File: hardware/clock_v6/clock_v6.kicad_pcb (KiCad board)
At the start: 2 copper layers, 130 x 70 mm, 241 parts, among them J1 RJ45, J12 Conn_01x06, J2 Conn_01x06_Pin, J3 Conn_01x05_Pin, J4 Conn_01x04_Pin, J5 Conn_01x06_Pin, J6 Conn_01x04_Pin, J7 Conn_01x04_Pin, J8 Conn_01x02, J9 Conn_02x10_Odd_Even, Q1 2N7002, Q10 2N7002, Q2 2N7002, Q3 2N7002, Q4 2N7002, Q5 2N7002, Q6 2N7002, Q7 2N7002, Q8 2N7002, Q9 2N7002, U1 ADA4807-1, U10 STM32F405RGTx, U11 AMS1117-3.3, U12 BA50DD0WHFP-TR, U13 M24C02-RMN, U2 SN74LVC1G14DBV, U3 SN74LVC1G14DBV, U4 ADA4807-1, U5 ADA4807-1, U6 TLV3603DCKR, U7 SN74LVC1G14DBV, U8 TLV3603DCKR, U9 L78L05_SOT89, X2 GTXO-14V (2.048MHz), Y1 AOCJY4A-10.000MHZ-SW, Y2 16MHz

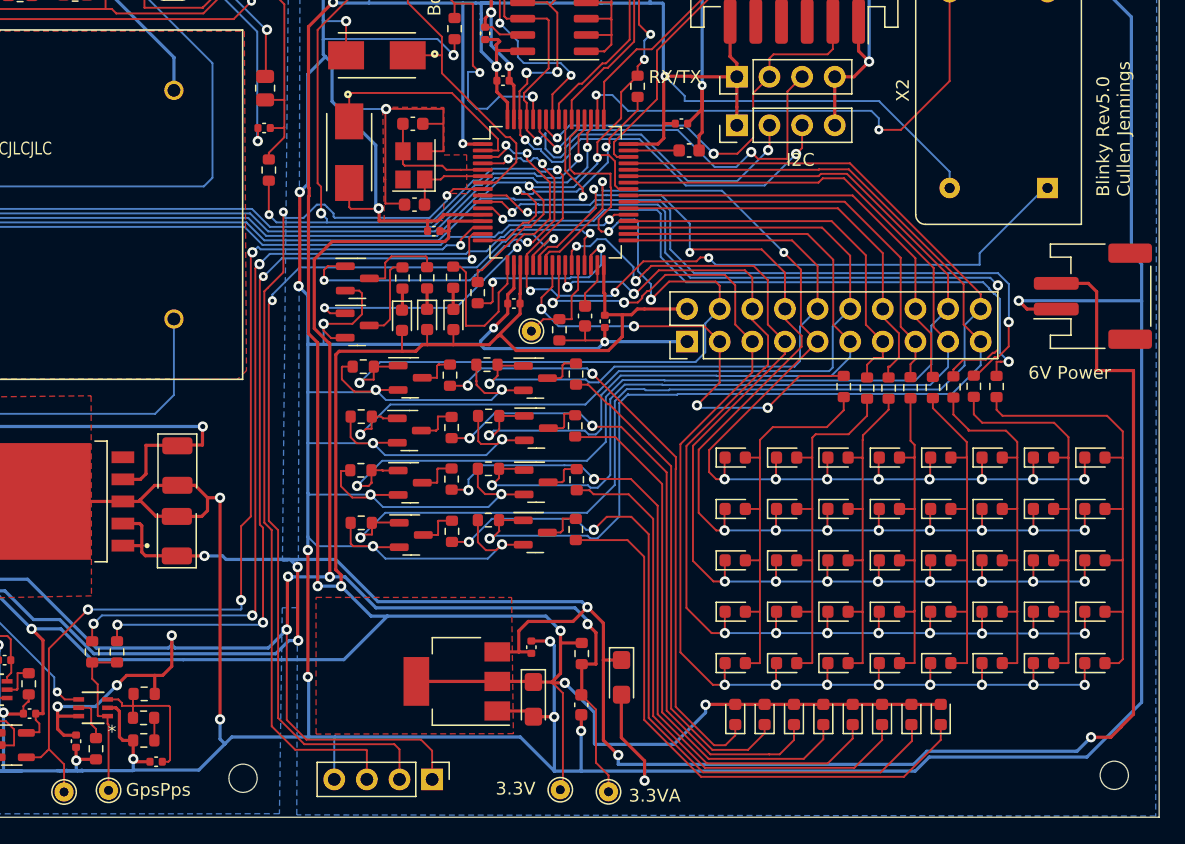
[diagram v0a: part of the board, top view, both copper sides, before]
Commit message: start cleaning up clock PCB
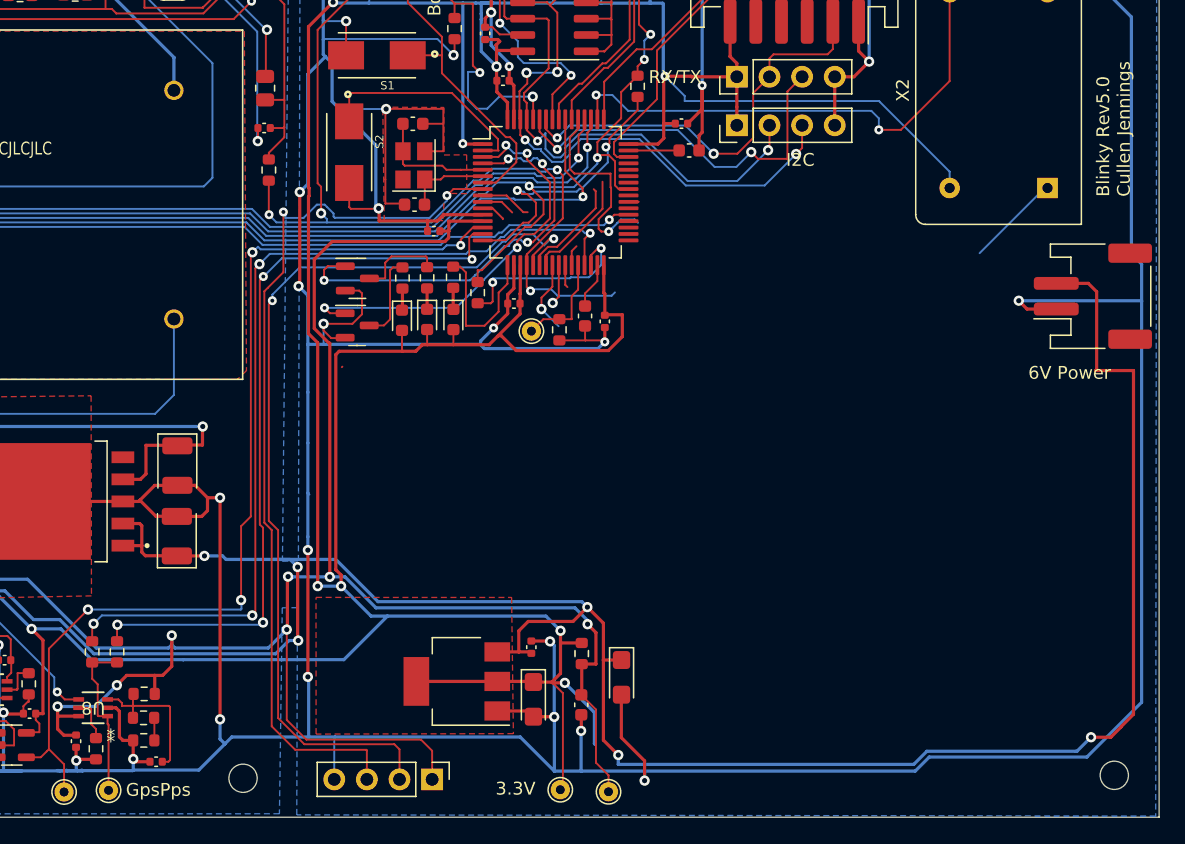
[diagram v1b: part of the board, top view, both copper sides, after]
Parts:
- removed D10, D11, D4, D5, D6, D7, D8, D9: LED-RED, LED_SMD:LED_0603_1608Metric
- removed D12, D13, D14, D15, D16, D17, D18, D19, D20, D21, D22, D23, D24, D25, D26, D27, D28, D29, D30, D31, D32, D33, D34, D35, D36, D37, D38, D39, D40, D41, D42, D43, D44, D45, D46, D47, D48, D49, D50, D51: LED-G, LED_SMD:LED_0603_1608Metric
- removed J9: Conn_02x10_Odd_Even, Connector_PinHeader_2.54mm:PinHeader_2x10_P2.54mm_Vertical
- removed Q1, Q2, Q3, Q4, Q5, Q6, Q7, Q8: 2N7002, Package_TO_SOT_SMD:SOT-23
- removed R33, R35, R37, R39, R41, R43, R45, R47: 4K7, Resistor_SMD:R_0603_1608Metric
- removed R34, R36, R38, R40, R42, R44, R46, R48: 100R, Resistor_SMD:R_0603_1608Metric
- removed R49, R50, R51, R52, R53, R55, R56, R57: 82R, Resistor_SMD:R_0603_1608Metric
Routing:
- net GND: track 1188.4 -> 1071.5 mm, vias 59 -> 51
- net /LEDB: track 98.3 -> 0.00 mm, vias 1 -> 0
- net /COL3: track 96.3 -> 3.36 mm, vias 10 -> 1
- net /LEDD: track 90.8 -> 0.00 mm, vias 1 -> 0
- net /COL5: track 91.8 -> 1.78 mm, vias 10 -> 0
- net /LEDC: track 89.7 -> 0.00 mm, vias 1 -> 0
- net /COL4: track 89.4 -> 1.63 mm, vias 10 -> 0
- net /COL1: track 94.0 -> 8.21 mm, vias 10 -> 0
- net /COL2: track 90.3 -> 8.78 mm, vias 10 -> 0
- net /LEDE: track 81.5 -> 0.00 mm, vias 1 -> 0
- net /LEDF: track 70.4 -> 0.00 mm, vias 1 -> 0
- net /LEDG: track 61.4 -> 0.00 mm, vias 1 -> 0
- net /LB: track 56.4 -> 0.00 mm, vias 2 -> 0
- net /LD: track 53.6 -> 0.00 mm, vias 2 -> 0
- net /LEDH: track 52.4 -> 0.00 mm, vias 1 -> 0
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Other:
- board text removed: "3.3VA"

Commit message: final clean up
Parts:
- removed ANT6: U.FL-R-SMT-1, blinky_footprints:U.FL-R-SMT-1
- removed J3: Conn_01x05_Pin, Connector_PinHeader_2.54mm:PinHeader_1x05_P2.54mm_Vertical
- removed JP1: SolderJumper_2_Bridged, Jumper:SolderJumper-2_P1.3mm_Bridged_RoundedPad1.0x1.5mm
- removed RV1: 20K, Potentiometer_SMD:Potentiometer_Bourns_3314G_Vertical
- removed TP12, TP13, TP14: ~, TestPoint:TestPoint_THTPad_D1.5mm_Drill0.7mm
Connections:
- R12 pad 2: Net-(J3-Pin_4) -> /Vadj
- R13 pad 1: Net-(J3-Pin_4) -> /Vadj
- R23 pad 2: Net-(J3-Pin_4) -> /Vadj
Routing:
- net +3.3VA: track 229.6 -> 136.7 mm, vias 9 -> 7
- net Net-(J3-Pin_4): track 50.4 -> 0.00 mm, vias 4 -> 0
- net Net-(Y1-VREF): track 59.8 -> 36.7 mm
- net OSC_ADJ: track 76.6 -> 60.2 mm, vias 4 -> 3
- net /LEDA: track 15.8 -> 0.00 mm, vias 1 -> 0
- net Net-(C26-Pad1): track 21.6 -> 7.74 mm, vias 1 -> 0
- net GND: track 1071.5 -> 1062.3 mm, vias 51 -> 50
- net /COL2: track 8.78 -> 0.00 mm
- net /COL1: track 8.21 -> 0.00 mm
- net +3.3V: track 374.3 -> 367.5 mm, vias 16 -> 15
- net /BOOT0: track 24.5 -> 18.8 mm
- net /ROW5: track 5.66 -> 0.00 mm, vias 1 -> 0
- net /Vadj: track 49.4 -> 44.3 mm, vias 2 -> 4
- net /ROW6: track 4.04 -> 0.00 mm
- net /NRST: track 28.4 -> 24.6 mm
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
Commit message: remove cheap osc
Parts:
- removed TP11: ~, TestPoint:TestPoint_THTPad_D1.5mm_Drill0.7mm
- removed X2: GTXO-14V (2.048MHz), Oscillator:Oscillator_DIP-14
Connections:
- TP10 pad 1: AUX_CLK -> CLK
- U10 pad 14: AUX_CLK -> /AUX_CLK
- U10 pad 50: /CLK -> CLK
- U7 pad 4: AUX_CLK -> CLK
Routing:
- net AUX_CLK: track 77.2 -> 0.00 mm, vias 4 -> 0
- net (no net): track 0.00 -> 77.2 mm, vias 0 -> 4
- net CLK: track 0.00 -> 39.6 mm, vias 0 -> 2
- net /CLK: track 39.6 -> 0.00 mm, vias 2 -> 0

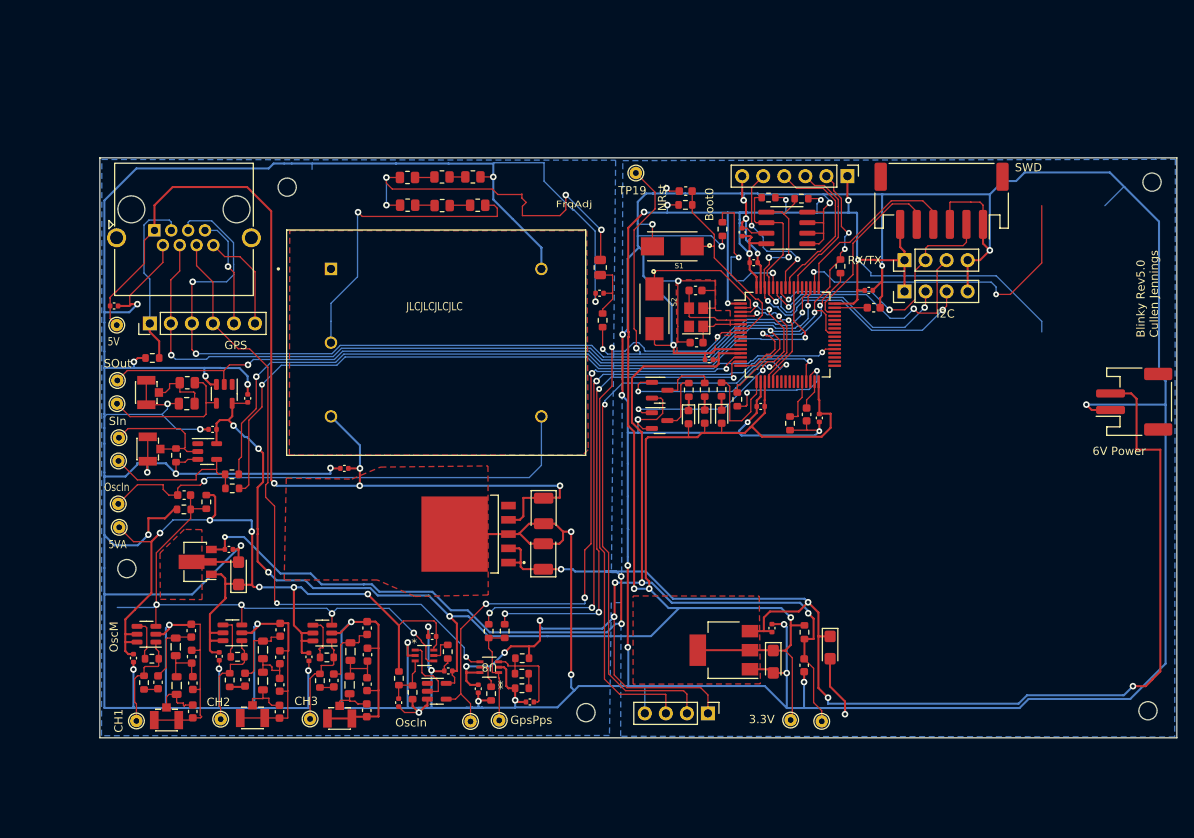
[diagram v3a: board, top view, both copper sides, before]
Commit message: clean up connections and add gps tx voltage dividers
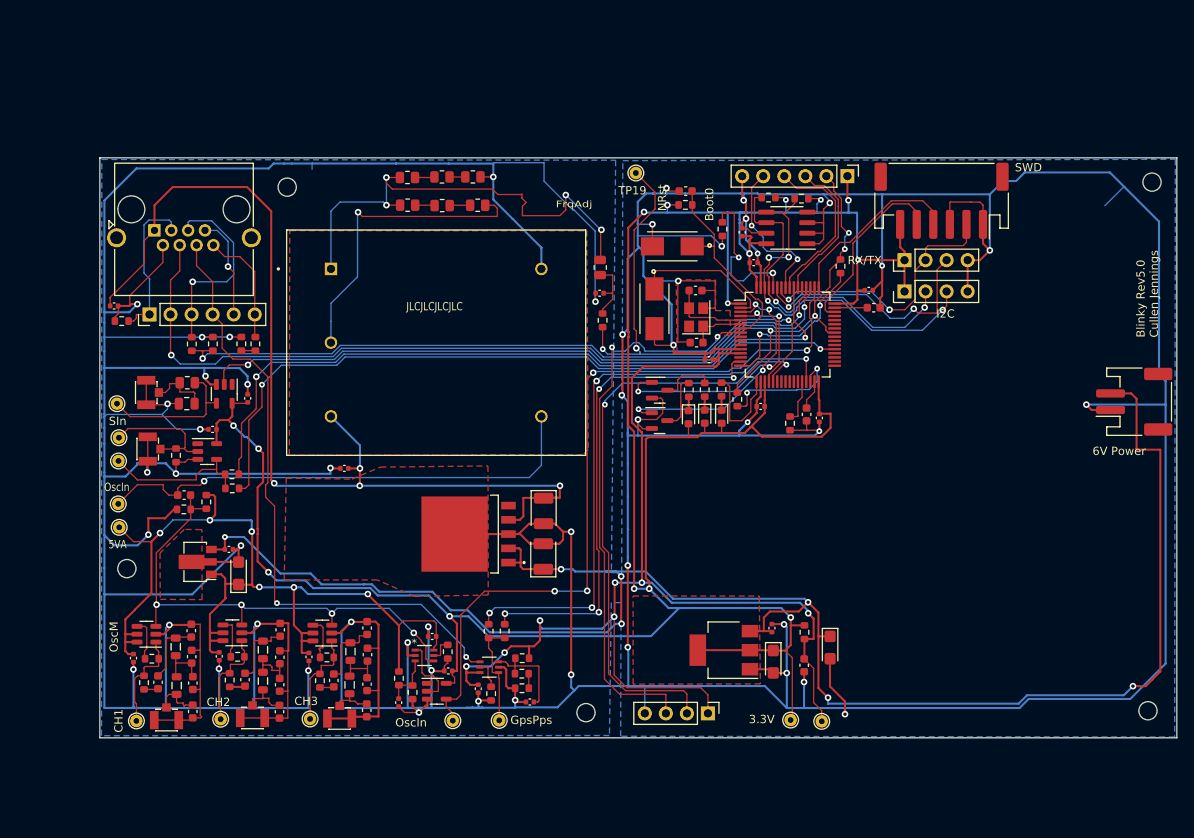
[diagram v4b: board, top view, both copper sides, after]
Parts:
- removed TP1, TP18: ~, TestPoint:TestPoint_THTPad_D1.5mm_Drill0.7mm
- added R33: 2K2, Resistor_SMD:R_0603_1608Metric, F.Cu at (118.8, 72.5)
- added R34: 4K7, Resistor_SMD:R_0603_1608Metric, F.Cu at (117.1, 72.4)
- added R35: 2K2, Resistor_SMD:R_0603_1608Metric, F.Cu at (111.1, 72.5)
- added R36: 4K7, Resistor_SMD:R_0603_1608Metric, F.Cu at (113.6, 72.5)
- moved R1 5.79 mm to (102.6, 69.7)
- moved TP10 2.14 mm to (142.6, 117.9)
- moved J2 1.08 mm to (106.0, 68.9)
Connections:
- net /GPS_TX2 renamed /GPS_TX2H
- J1 pad 5: /GPS_TX1 -> /GPS_TX1H
- J2 pad 3: /GPS_TX1 -> /GPS_TX1H
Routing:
- net (no net): track 77.2 -> 0.00 mm, vias 4 -> 0
- net CLK: track 39.6 -> 92.7 mm, vias 2 -> 4
- net +3.3V: track 367.5 -> 340.8 mm
- net /GPS_TX1H: track 0.00 -> 23.5 mm, vias 0 -> 1
- net /GPS_TX1: track 105.7 -> 82.9 mm, vias 3 -> 2
- net GND: track 1062.3 -> 1080.9 mm, vias 50 -> 51
- net SYNC_OUT: track 125.6 -> 109.6 mm
- net /Vadj: track 44.3 -> 58.6 mm
- net /10Mhz2.5V: track 65.8 -> 61.0 mm
- net +5V: track 122.2 -> 119.6 mm
- net /GPS_EN: track 21.5 -> 18.9 mm
- net /AUX_SYNC_MON: track 22.2 -> 20.2 mm
- net /GPS_TX2: track 0.00 -> 1.70 mm
- net /GPS_TX2H: track 12.6 -> 14.3 mm
- net /LEDM1: track 32.9 -> 31.6 mm
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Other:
- board text removed: "5V"
- board text removed: "GPS"
- board text removed: "SOut"

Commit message: resize board
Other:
- board size 130 x 70 mm -> 119 x 92 mm
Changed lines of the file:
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@@
     )
     (pad_to_mask_clearance 0)
-    (aux_axis_origin 100 120)
+    (aux_axis_origin 90 125)
     (pcbplotparams
       (layerselection 0x00010fc_ffffffff)
@@
     )
   )
-  (gr_line (start 230 120) (end 100 120)
+  (gr_line (start 209 125) (end 90 125)
     (stroke (width 0.1) (type default)) (layer "Edge.Cuts"))
-  (gr_line (start 100 50) (end 230 50)
+  (gr_line (start 90 33) (end 209 33)
     (stroke (width 0.1) (type default)) (layer "Edge.Cuts"))
-  (gr_line (start 230 50) (end 230 120)
+  (gr_line (start 209 33) (end 209 125)
     (stroke (width 0.1) (type default)) (layer "Edge.Cuts"))
-  (gr_line (start 100 50) (end 100 120)
+  (gr_line (start 90 33) (end 90 125)
     (stroke (width 0.1) (type default)) (layer "Edge.Cuts"))
   (gr_line (start 230 117.5) (end 100 117.5)

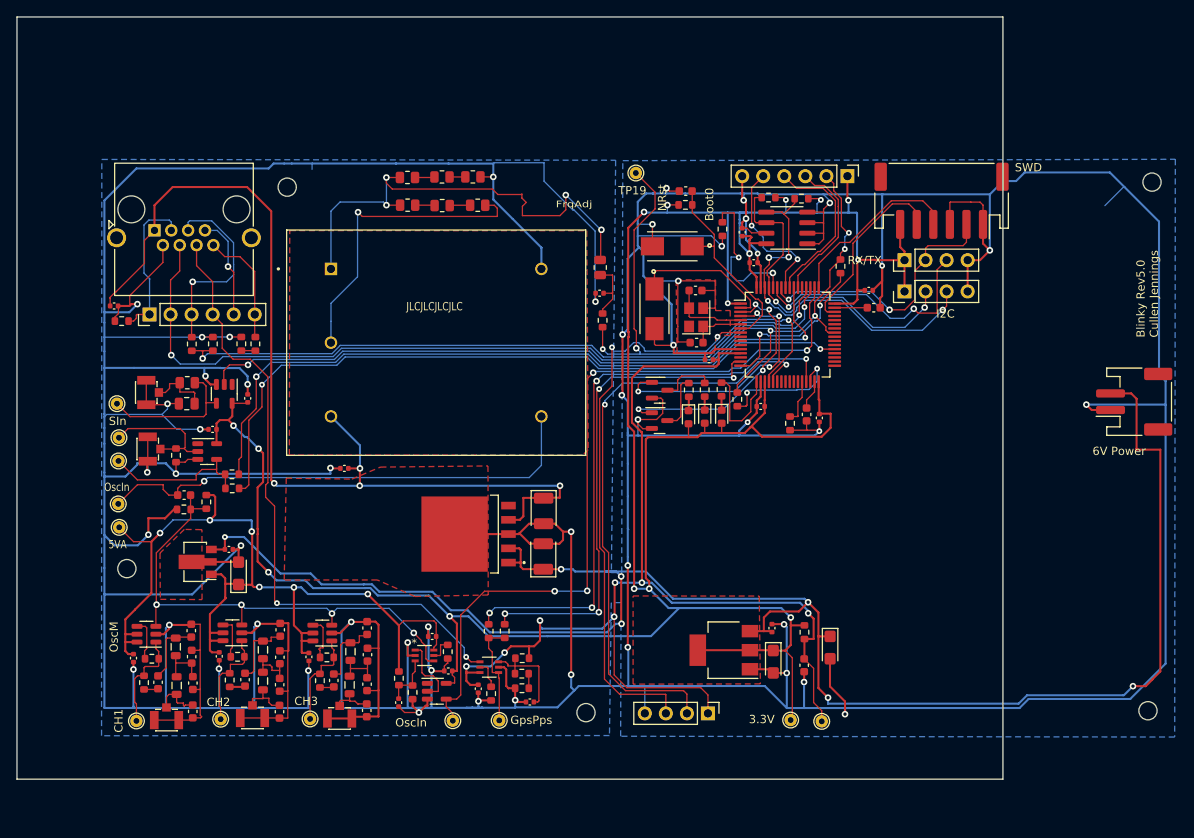
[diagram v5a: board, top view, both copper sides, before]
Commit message: move GPS connector to board edge
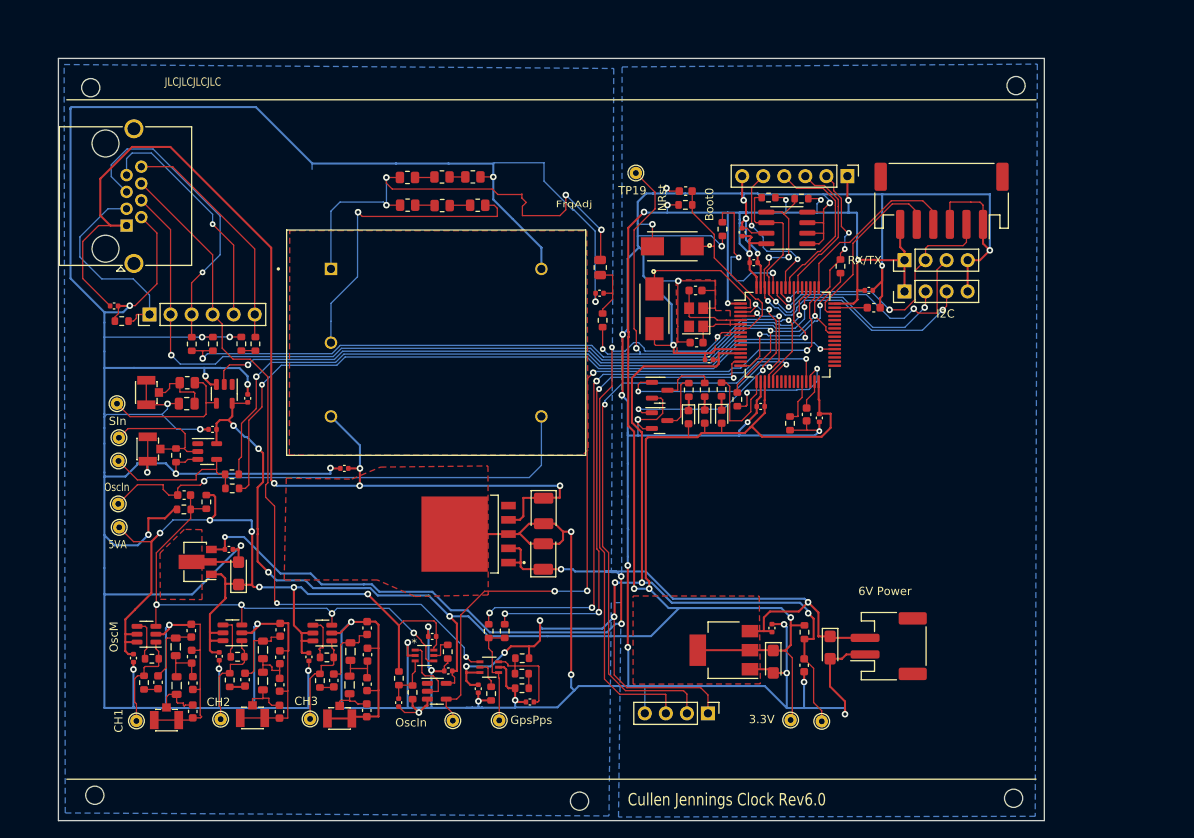
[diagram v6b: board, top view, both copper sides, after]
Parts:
- moved J8 41.8 mm to (195.2, 108.9)
- moved H5 27.6 mm to (99.4, 126.9)
- moved H1 26.6 mm to (98.9, 41.5)
- moved H2 20.1 mm to (210.6, 41.3)
- moved H4 19.4 mm to (210.3, 127.3)
- moved H3 10.7 mm to (157.9, 127.6)
- moved J1 3.42 mm to (103.2, 58.2), turned to 90 degrees
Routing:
- net GND: track 1080.9 -> 971.0 mm, vias 51 -> 50
- net +6V: track 211.6 -> 126.3 mm, vias 7 -> 5
- net /GPS_RX2: track 12.5 -> 28.9 mm
- net +5V: track 119.6 -> 135.1 mm
- net /GPS_TX2H: track 14.3 -> 28.5 mm
- net /GPS_TX1H: track 23.5 -> 37.4 mm
- net /GPS_EXT_PPS: track 76.6 -> 86.8 mm
- net /GPS_RX1: track 98.4 -> 104.8 mm
- net /GPS_EN: track 18.9 -> 25.2 mm
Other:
- board text added: "Cullen Jennings Clock Rev6.0"
- board text removed: "Blinky Rev5.0 Cullen Jennings"
- board text removed: "SWD"
